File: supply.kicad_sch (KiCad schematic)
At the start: 88 parts, among them SW1 SW_B3U-3000PM_SMD, U10 CSD86330Q3D, U4 PAC1934_QFN, U5 TPS2117DRLR, U6 TPS2117DRLR, U7 LMR62014XMF, U8 TPS65086100, U9 CSD86330Q3D

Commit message: [#54016] Change 100nF to 0201 package
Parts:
- C100, C101, C255, C256, C85, C86, C88: value C_100n_0402 -> C_100n_0201_25V; footprint antmicro-footprints:C_0402_1005Metric -> antmicro-footprints:C_0201; symbol antmicroCapacitors0402:C_100n_0402 -> antmicroCapacitorsmisc:C_100n_0201_25V; MPN GRM155R61H104KE14D -> C0603X5R1E104K030BB; Manufacturer Murata -> TDK; Voltage 50V -> 25V

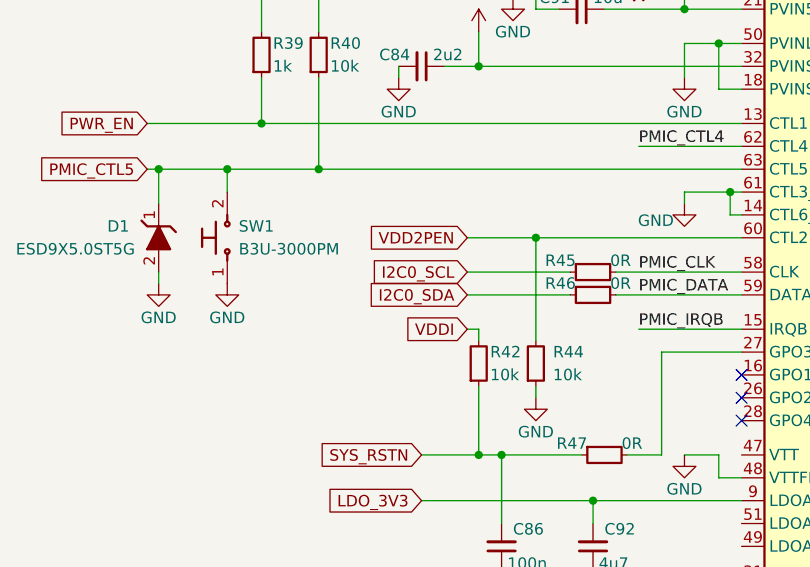
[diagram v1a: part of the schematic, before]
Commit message: [#54016] Add PMIC to MSSIO I2C_1
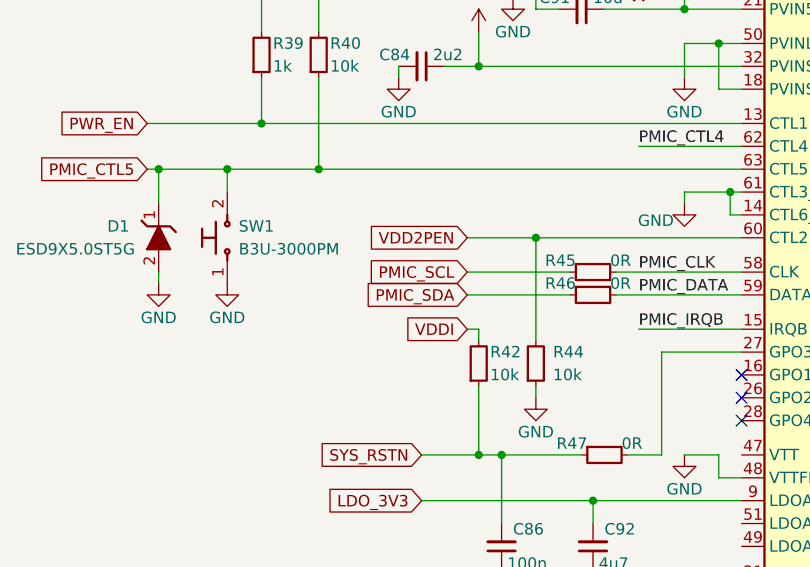
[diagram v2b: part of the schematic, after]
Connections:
- net I2C0_SCL renamed PMIC_SCL
- net I2C0_SDA renamed PMIC_SDA
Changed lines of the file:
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@@
     )
   )
-  (global_label "I2C0_SDA" (shape input) (at 182.88 88.9 180) (fields_autoplaced)
+  (global_label "PMIC_SDA" (shape input) (at 182.88 88.9 180) (fields_autoplaced)
     (effects (font (size 1.27 1.27)) (justify right))
-    (property "Intersheetrefs" "${INTERSHEET_REFS}" (at 65.405 -34.925 0)
-      (effects (font (size 1.27 1.27)) hide)
+    (property "Intersheetrefs" "${INTERSHEET_REFS}" (at 170.7629 88.9 0)
+      (effects (font (size 1.27 1.27)) (justify right) hide)
     )
   )
@@
     )
   )
-  (global_label "I2C0_SCL" (shape input) (at 182.88 86.36 180) (fields_autoplaced)
+  (global_label "PMIC_SCL" (shape input) (at 182.88 86.36 180) (fields_autoplaced)
     (effects (font (size 1.27 1.27)) (justify right))
-    (property "Intersheetrefs" "${INTERSHEET_REFS}" (at 65.405 -34.925 0)
-      (effects (font (size 1.27 1.27)) hide)
+    (property "Intersheetrefs" "${INTERSHEET_REFS}" (at 170.8234 86.36 0)
+      (effects (font (size 1.27 1.27)) (justify right) hide)
     )
   )

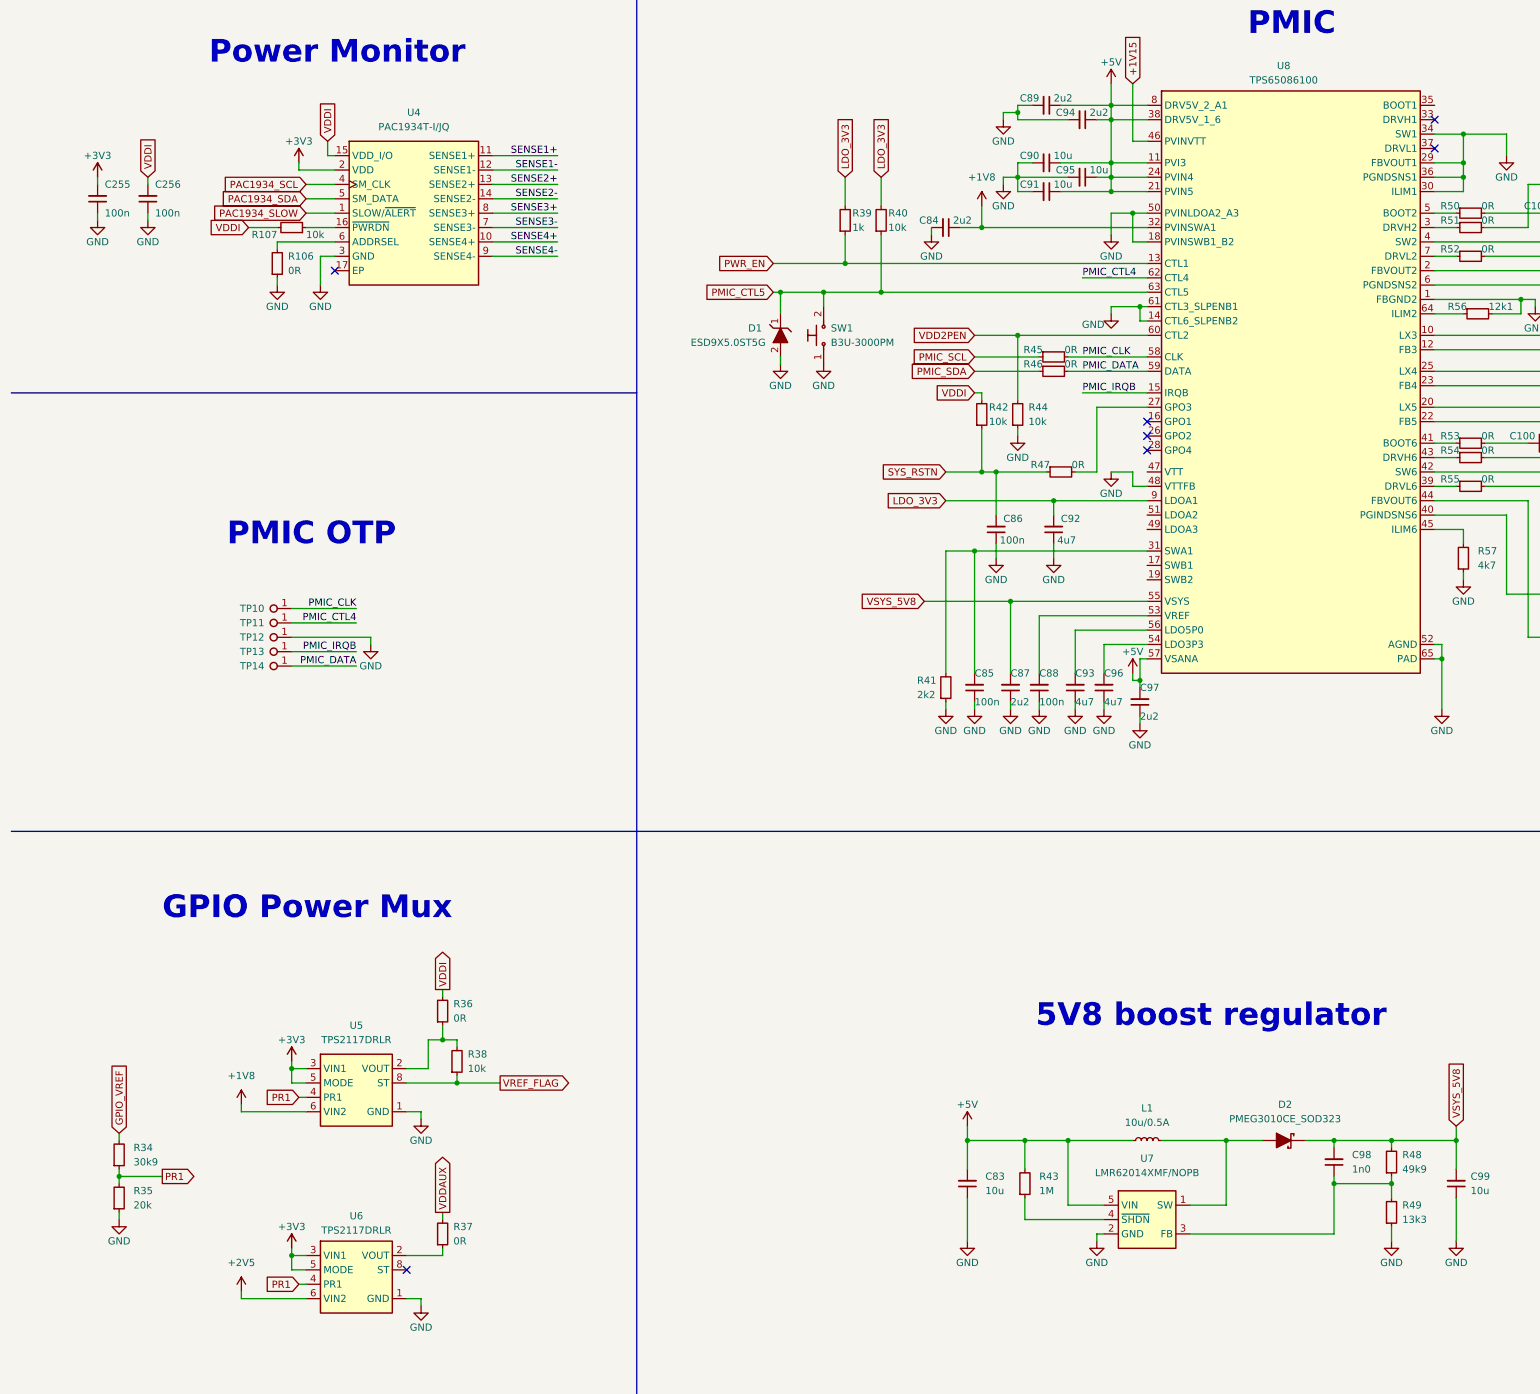
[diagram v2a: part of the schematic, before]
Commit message: [#54899] Add power sequencing to Power Mux
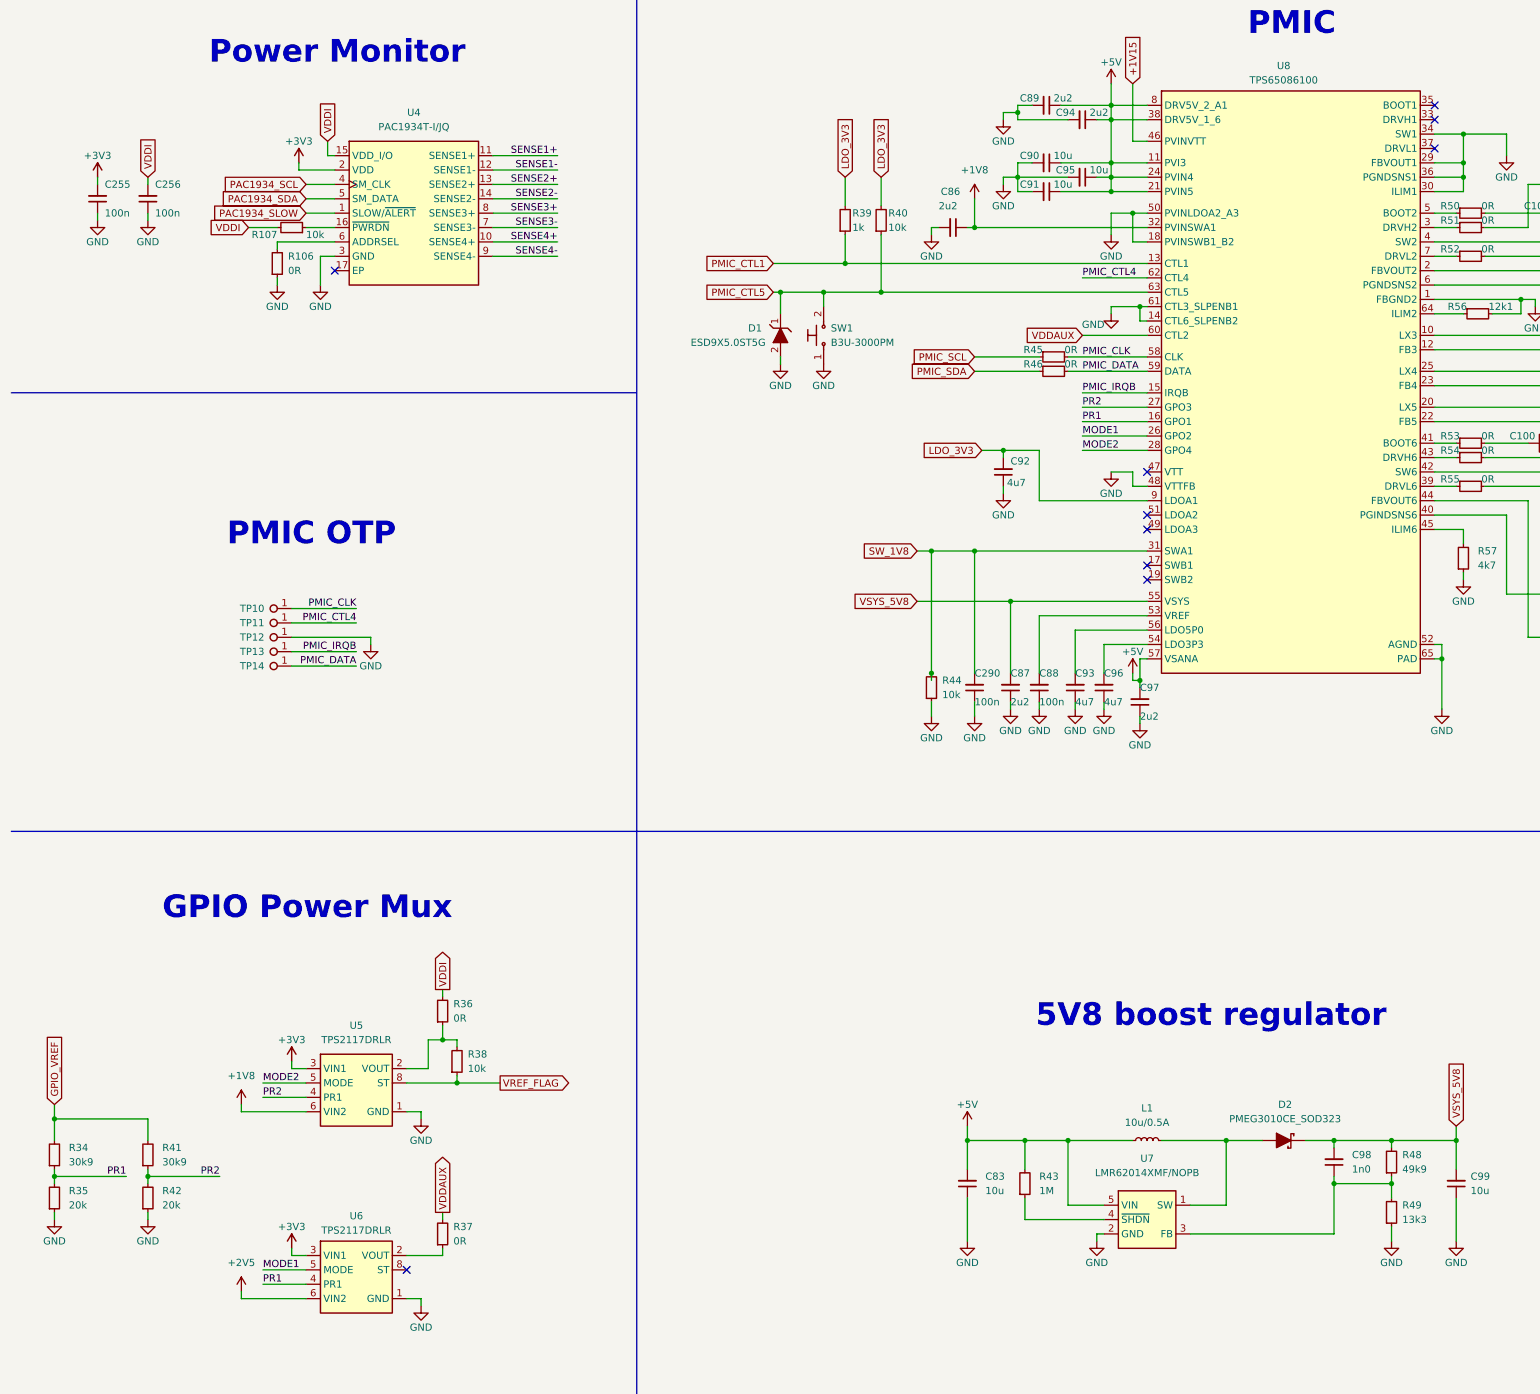
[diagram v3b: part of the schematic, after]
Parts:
- removed C84: C_2u2_0402, antmicro-footprints:C_0402_1005Metric, symbol antmicroCapacitors0402:C_2u2_0402
- removed C85, C86: C_100n_0201_25V, antmicro-footprints:C_0201, symbol antmicroCapacitorsmisc:C_100n_0201_25V
- removed R41: R_2k2_0402, antmicro-footprints:R_0402_1005Metric, symbol antmicroResistors0402:R_2k2_0402
- removed R42: R_10k_0402, antmicro-footprints:R_0402_1005Metric, symbol antmicroResistors0402:R_10k_0402
- removed R47: R_0R_0402, antmicro-footprints:R_0402_1005Metric, symbol antmicroResistors0402:R_0R_0402
- added C290: C_100n_0201_25V, antmicro-footprints:C_0201, symbol antmicroCapacitorsmisc:C_100n_0201_25V
- added C86: C_2u2_0402, antmicro-footprints:C_0402_1005Metric, symbol antmicroCapacitors0402:C_2u2_0402
- added R41: R_30k9_0402, antmicro-footprints:R_0402_1005Metric, symbol antmicroResistors0402:R_30k9_0402
- added R42: R_20k_0402, antmicro-footprints:R_0402_1005Metric, symbol antmicroResistors0402:R_20k_0402
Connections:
- net +1V8: now also C86.1
- net +3V3: no longer U5.5 (MODE), U6.5 (MODE)
- net GND: now also C290.1, C86.2, R42.1
- net GPIO_VREF: now also R41.2
- net PR1: now also U8.16 (GPO1); no longer U5.4 (PR1)
- net VDDAUX: now also U8.60 (CTL2)
- net MODE1: now reaches U8.26 (GPO2)
- net MODE1: now also U6.5 (MODE)
- net PR2: now reaches U8.27 (GPO3)
- net PR2: now also U5.4 (PR1), R41.1, R42.2
- net MODE2: now reaches U8.28 (GPO4)
- net MODE2: now also U5.5 (MODE)
- net SW_1V8: now reaches U8.31 (SWA1)
- net SW_1V8: now also R44.2, C290.2
- net PWR_EN renamed PMIC_CTL1
- removed net VDD2PEN: R44.2, U8.60 (CTL2)
- no-connect marks 7 -> 10
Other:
- moved on the sheet: C92, R34, R35

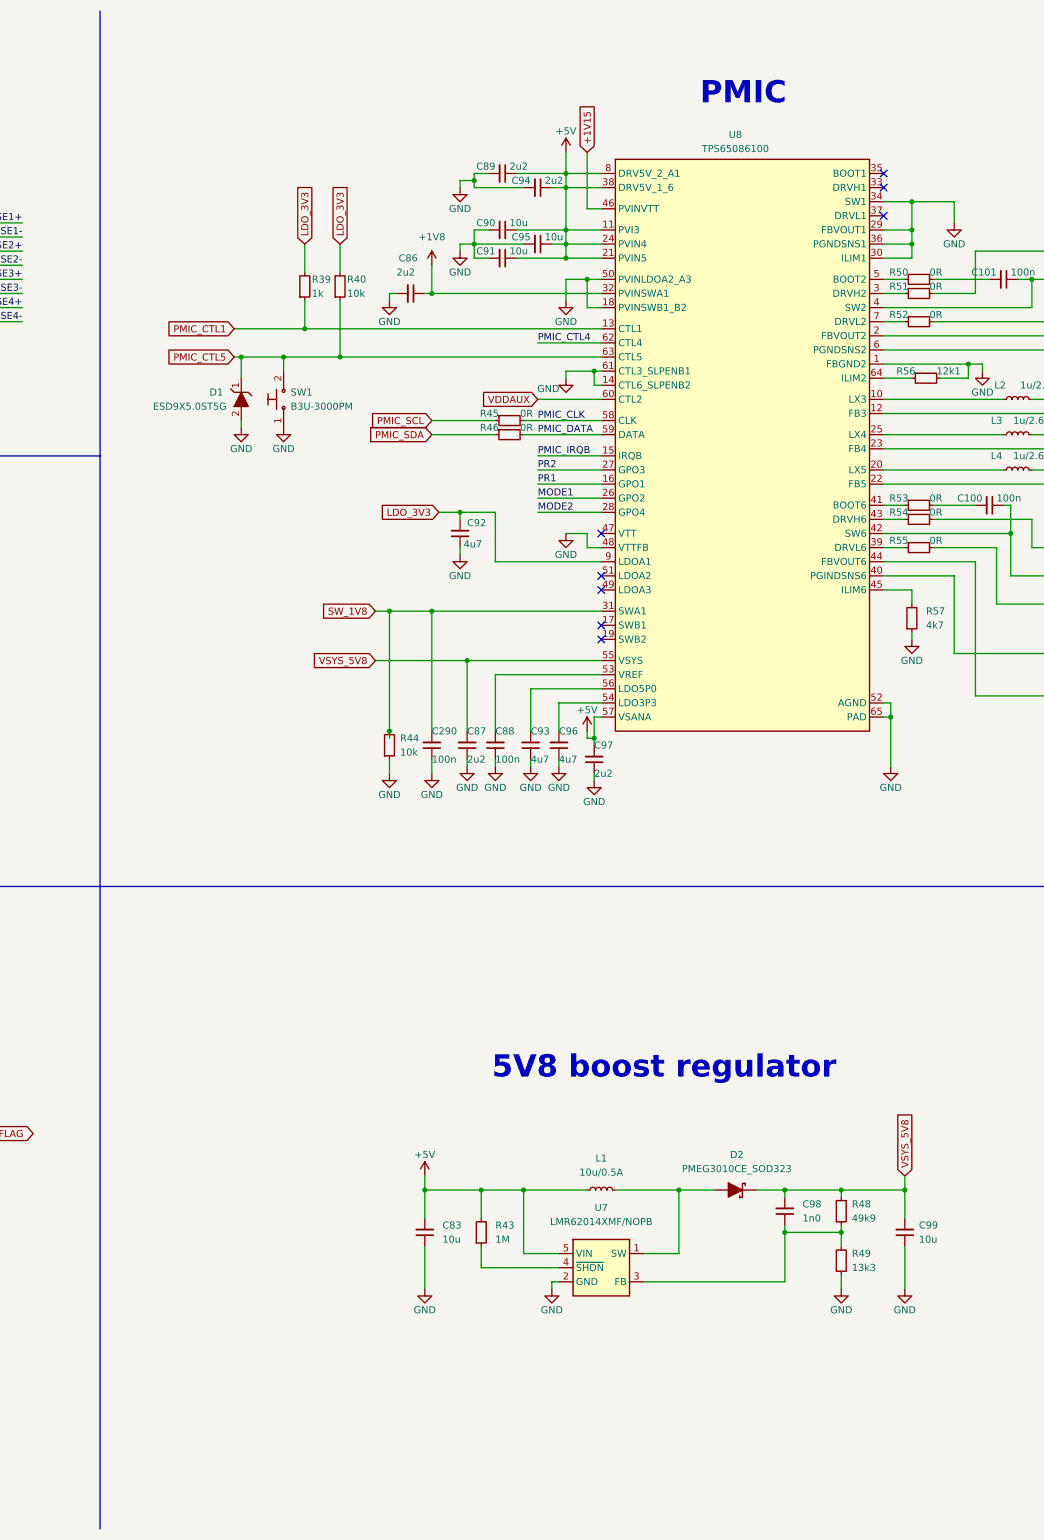
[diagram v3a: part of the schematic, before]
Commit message: [#54899] Simplify power sequencing, add missing connections
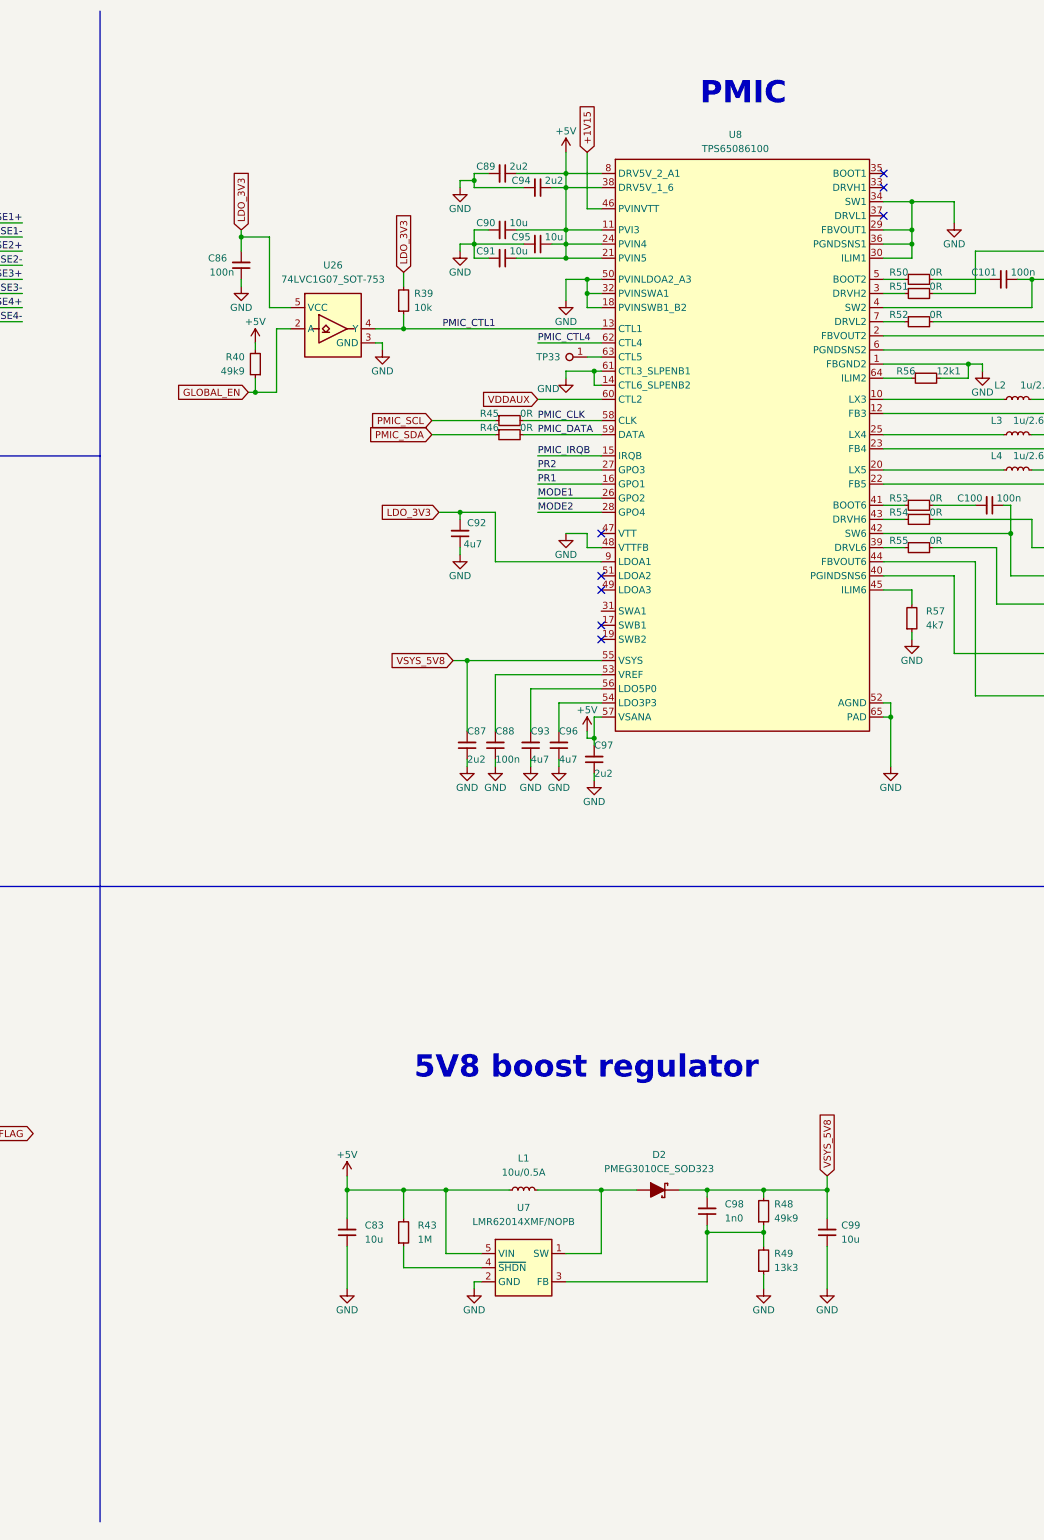
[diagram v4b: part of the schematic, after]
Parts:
- removed C290: C_100n_0201_25V, antmicro-footprints:C_0201, symbol antmicroCapacitorsmisc:C_100n_0201_25V
- removed C86: C_2u2_0402, antmicro-footprints:C_0402_1005Metric, symbol antmicroCapacitors0402:C_2u2_0402
- removed D1: ESD9X5.0ST5G, antmicro-footprints:SOD-923, symbol antmicroTVSDiodes:ESD9X5.0ST5G
- removed R39: R_1k_0402, antmicro-footprints:R_0402_1005Metric, symbol antmicroResistors0402:R_1k_0402
- removed R40, R44: R_10k_0402, antmicro-footprints:R_0402_1005Metric, symbol antmicroResistors0402:R_10k_0402
- removed SW1: SW_B3U-3000PM_SMD, antmicro-footprints:SW_B3U-3000PM_SMD, symbol antmicroPushbuttonSwitches:SW_B3U-3000PM_SMD
- added C86: C_100n_0201_25V, antmicro-footprints:C_0201, symbol antmicroCapacitorsmisc:C_100n_0201_25V
- added R39: R_10k_0402, antmicro-footprints:R_0402_1005Metric, symbol antmicroResistors0402:R_10k_0402
- added R40: R_49k9_0402, antmicro-footprints:R_0402_1005Metric, symbol antmicroResistors0402:R_49k9_0402
- added TP33: TP_0.75mm_SMD, antmicro-footprints:TP_SMD_0.75mm, symbol antmicroTestPoints:TP_0.75mm_SMD
- added U26: 74LVC1G07_SOT-753, antmicro-footprints:SOT-753, symbol antmicroLogicBuffersDriversReceiversTransceivers:74LVC1G07_SOT-753
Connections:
- net +1V8: no longer U8.32 (PVINSWA1)
- net +5V: now also R40.2
- net GND: now also U8.32 (PVINSWA1), C86.1, U26.3 (GND)
- net LDO_3V3: now also C86.2, R39.2, U26.5 (VCC)
- net PMIC_CTL1: now also R39.1, U26.4 (Y)
- net PMIC_CTL5: no longer names the net of U8.63 (CTL5)
- net PMIC_CTL5: now also TP33.1
- net SW_1V8: no longer names the net of U8.31 (SWA1)
- new net GLOBAL_EN: R40.1, U26.2 (A)
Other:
- moved on the sheet: C83, C98, C99, D2, L1, R43, R48, R49, U7
